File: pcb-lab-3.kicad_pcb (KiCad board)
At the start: 2 copper layers, 0 parts

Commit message: Approx layout of 1st circuit
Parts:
- added C1: 0.1u, local_footprints:0805_HS, F.Cu at (149.9, 45.7)
- added C2: 1u, local_footprints:1206_HS, F.Cu at (132.7, 40.6)
- added C3: 0.1u, local_footprints:0805_HS, F.Cu at (141.0, 36.8)
- added C301: 0.1u, local_footprints:0805_HS, F.Cu at (127.6, 98.1)
- added C302: 0.1u, local_footprints:0805_HS, F.Cu at (145.1, 80.0)
- added C303: 1u, local_footprints:1206_HS, F.Cu at (127.1, 92.1)
- added C304: 0.1u, local_footprints:0805_HS, F.Cu at (137.9, 87.8)
- added C305: 0.1u, local_footprints:0805_HS, F.Cu at (145.1, 77.1)
- added C4: 0.1u, local_footprints:0805_HS, F.Cu at (146.1, 36.8)
- added C401: 0.1u, local_footprints:0805_HS, F.Cu at (133.4, 111.6)
- added C402: 1u, local_footprints:1206_HS, F.Cu at (130.7, 104.3)
- added C403: 1u, local_footprints:1206_HS, F.Cu at (116.2, 121.3)
- added C404: 1u, local_footprints:1206_HS, F.Cu at (124.0, 113.0)
- added C405: 0.1u, local_footprints:0805_HS, F.Cu at (125.6, 120.6)
- added C406: 0.1u, local_footprints:0805_HS, F.Cu at (128.1, 116.8)
- added J1: USB_B_Micro, local_footprints:USB-micro-B_4-legs_Banggood, F.Cu at (121.9, 40.6)
- added J2: Conn_01x02, local_footprints:Pin_Header_Straight_1x02_Pitch2.54mm, F.Cu at (130.2, 39.4)
- added J3: Conn_01x02, local_footprints:Pin_Header_Straight_1x02_Pitch2.54mm, F.Cu at (161.9, 36.8)
- added J301: USB_B_Micro, local_footprints:USB-micro-B_4-legs_Banggood, F.Cu at (111.6, 92.7)
- added J302: USB_B_Micro, local_footprints:USB-micro-B_4-legs_Banggood, F.Cu at (111.6, 83.5)
- added J303: Conn_01x02, local_footprints:Pin_Header_Straight_1x02_Pitch2.54mm, F.Cu at (126.1, 88.7)
- added J304: Conn_01x02, local_footprints:Pin_Header_Straight_1x02_Pitch2.54mm, F.Cu at (122.5, 92.6)
- added J305: Conn_01x02, local_footprints:Pin_Header_Straight_1x02_Pitch2.54mm, F.Cu at (133.9, 80.0)
- added J306: Conn_01x02, local_footprints:Pin_Header_Straight_1x02_Pitch2.54mm, F.Cu at (137.5, 80.0)
- added J307: Conn_01x02, local_footprints:Pin_Header_Straight_1x02_Pitch2.54mm, F.Cu at (122.5, 86.5)
- added J308: Conn_01x02, local_footprints:Pin_Header_Straight_1x02_Pitch2.54mm, F.Cu at (141.1, 80.0)
- added J309: Conn_01x03_Female, local_footprints:Pin_Header_Straight_1x03_Pitch2.54mm, F.Cu at (127.7, 82.6)
- added J310: Conn_01x02_Female, local_footprints:Pin_Header_Straight_1x02_Pitch2.54mm, F.Cu at (133.9, 86.2)
- added J311: Conn_01x03_Female, local_footprints:Pin_Header_Straight_1x03_Pitch2.54mm, F.Cu at (118.9, 89.0)
- added J4: Conn_01x02, local_footprints:Pin_Header_Straight_1x02_Pitch2.54mm, F.Cu at (161.9, 41.9)
- added J401: USB_B_Micro, local_footprints:USB-micro-B_4-legs_Banggood, F.Cu at (111.6, 110.4)
- added J402: Conn_01x02, local_footprints:Pin_Header_Straight_1x02_Pitch2.54mm, F.Cu at (111.6, 122.7)
- added J403: Conn_01x02, local_footprints:Pin_Header_Straight_1x02_Pitch2.54mm, F.Cu at (126.1, 107.0)
- added J404: Conn_01x02, local_footprints:Pin_Header_Straight_1x02_Pitch2.54mm, F.Cu at (119.4, 115.7)
- added J405: Conn_01x03, local_footprints:Pin_Header_Straight_1x03_Pitch2.54mm, F.Cu at (122.5, 109.5)
- added J406: Conn_01x03_Female, local_footprints:Pin_Header_Straight_1x03_Pitch2.54mm, F.Cu at (118.9, 109.5)
- added J407: Conn_01x02, local_footprints:Pin_Header_Straight_1x02_Pitch2.54mm, F.Cu at (108.0, 122.7)
- added J5: Conn_01x03, local_footprints:Pin_Header_Straight_1x03_Pitch2.54mm, F.Cu at (142.2, 49.5)
- added J501: Conn_01x02, local_footprints:Pin_Header_Straight_1x02_Pitch2.54mm, F.Cu at (157.7, 107.0)
- added J502: Conn_01x02, local_footprints:Pin_Header_Straight_1x02_Pitch2.54mm, F.Cu at (161.3, 107.0)
- added J503: Conn_01x02, local_footprints:Pin_Header_Straight_1x02_Pitch2.54mm, F.Cu at (154.1, 107.0)
- added J6: Conn_01x04, local_footprints:Pin_Header_Straight_1x04_Pitch2.54mm, F.Cu at (123.2, 48.3)
- added JP1: SolderJumper_2_Open, Jumper:SolderJumper-2_P1.3mm_Open_RoundedPad1.0x1.5mm, F.Cu at (137.8, 41.9)
- added JP2: SolderJumper_2_Open, Jumper:SolderJumper-2_P1.3mm_Open_RoundedPad1.0x1.5mm, F.Cu at (151.1, 39.4)
- added JP301: SolderJumper_2_Open, Jumper:SolderJumper-2_P1.3mm_Open_RoundedPad1.0x1.5mm, F.Cu at (145.5, 91.0)
- added JP302: SolderJumper_2_Open, Jumper:SolderJumper-2_P1.3mm_Open_RoundedPad1.0x1.5mm, F.Cu at (140.9, 94.6)
- added JP303: SolderJumper_2_Open, Jumper:SolderJumper-2_P1.3mm_Open_RoundedPad1.0x1.5mm, F.Cu at (141.2, 91.0)
- added JP304: SolderJumper_2_Open, Jumper:SolderJumper-2_P1.3mm_Open_RoundedPad1.0x1.5mm, F.Cu at (136.3, 97.2)
- added JP401: SolderJumper_2_Open, Jumper:SolderJumper-2_P1.3mm_Open_RoundedPad1.0x1.5mm, F.Cu at (129.9, 120.0)
- added JP402: SolderJumper_2_Open, Jumper:SolderJumper-2_P1.3mm_Open_RoundedPad1.0x1.5mm, F.Cu at (140.1, 109.1)
- added JP403: SolderJumper_2_Open, Jumper:SolderJumper-2_P1.3mm_Open_RoundedPad1.0x1.5mm, F.Cu at (133.3, 114.8)
- added Q1: Q_NMOS_GSD, local_footprints:SOT-23_HS, F.Cu at (157.5, 40.6)
- added Q301: Q_NMOS_GSD, local_footprints:SOT-23_HS, F.Cu at (132.2, 90.2)
- added Q302: Q_NMOS_GSD, local_footprints:SOT-23_HS, F.Cu at (138.1, 84.1)
- added Q401: Q_NMOS_GSD, local_footprints:SOT-23_HS, F.Cu at (123.5, 116.9)
- added R1: 100k, local_footprints:0805_HS, F.Cu at (129.5, 48.3)
- added R2: 1k, local_footprints:0805_HS, F.Cu at (139.7, 41.9)
- added R3: 100k, local_footprints:0805_HS, F.Cu at (149.9, 50.2)
- added R301: 1k, local_footprints:0805_HS, F.Cu at (136.5, 94.0)
- added R302: 1k, local_footprints:0805_HS, F.Cu at (132.0, 96.8)
- added R303: 100k, local_footprints:0805_HS, F.Cu at (142.3, 87.8)
- added R304: 100k, local_footprints:0805_HS, F.Cu at (136.8, 90.7)
- added R305: 1, local_footprints:1210_HS, F.Cu at (109.0, 96.0)
- added R306: 1k, local_footprints:0805_HS, F.Cu at (132.1, 94.0)
- added R307: 1k, local_footprints:0805_HS, F.Cu at (142.6, 83.3)
- added R308: 100k, local_footprints:0805_HS, F.Cu at (127.6, 95.2)
- added R309: 1, local_footprints:1210_HS, F.Cu at (122.6, 96.2)
- added R4: 3.3k, local_footprints:0805_HS, F.Cu at (149.9, 52.7)
- added R401: 3.3k, local_footprints:0805_HS, F.Cu at (140.8, 104.1)
- added R402: 3.3k, local_footprints:0805_HS, F.Cu at (135.7, 108.7)
- added R403: 100k, local_footprints:0805_HS, F.Cu at (129.0, 113.9)
- added R404: 1k, local_footprints:0805_HS, F.Cu at (129.0, 111.0)
- added R405: 1k, local_footprints:0805_HS, F.Cu at (121.2, 120.6)
- added R406: 100k, local_footprints:0805_HS, F.Cu at (121.2, 123.5)
- added R407: 1, local_footprints:1210_HS, F.Cu at (130.7, 107.7)
- added R5: 1k, local_footprints:0805_HS, F.Cu at (151.1, 36.8)
- added R6: 100k, local_footprints:0805_HS, F.Cu at (156.2, 36.8)
- added R7: 1, local_footprints:1210_HS, F.Cu at (146.1, 51.4)
- added RV1: 50k, local_footprints:Conn_01x03_small, F.Cu at (138.4, 52.1)
- added RV301: 100k, local_footprints:Conn_01x03_small, F.Cu at (130.8, 79.6)
- added RV302: 10k, local_footprints:Conn_01x03_small, F.Cu at (118.4, 94.7)
- added RV401: 1k, local_footprints:Conn_01x03_small, F.Cu at (116.3, 115.8)
- added RV501: 100, local_footprints:Conn_01x03_small, F.Cu at (151.0, 106.5)
- added TP1: TestPoint, local_footprints:SMD-Pad_01x01, F.Cu at (135.9, 45.1)
- added TP401: TestPoint, local_footprints:SMD-Pad_01x01, F.Cu at (125.5, 123.3)
- added TP402: TestPoint, local_footprints:SMD-Pad_01x01, F.Cu at (137.7, 112.2)
- added U1: NCS2333, local_footprints:SOIC-8_3.9x4.9mm_Pitch1.27mm_HS, F.Cu at (144.8, 43.2)
- added U2: MCP4011, local_footprints:SOIC-8_3.9x4.9mm_Pitch1.27mm_HS, F.Cu at (129.5, 52.1)
- added U301: NCS2333, local_footprints:SOIC-8_3.9x4.9mm_Pitch1.27mm_HS, F.Cu at (121.5, 78.9)
- added U302: INA181, local_footprints:SOT-23-6_HS, F.Cu at (114.3, 96.5)
- added U401: NCS2333, local_footprints:SOIC-8_3.9x4.9mm_Pitch1.27mm_HS, F.Cu at (110.6, 115.1)
- added U402: INA181, local_footprints:SOT-23-6_HS, F.Cu at (136.0, 105.0)
- added U501: BCR421U, local_footprints:SOT-23-6_HS, F.Cu at (165.7, 105.0)

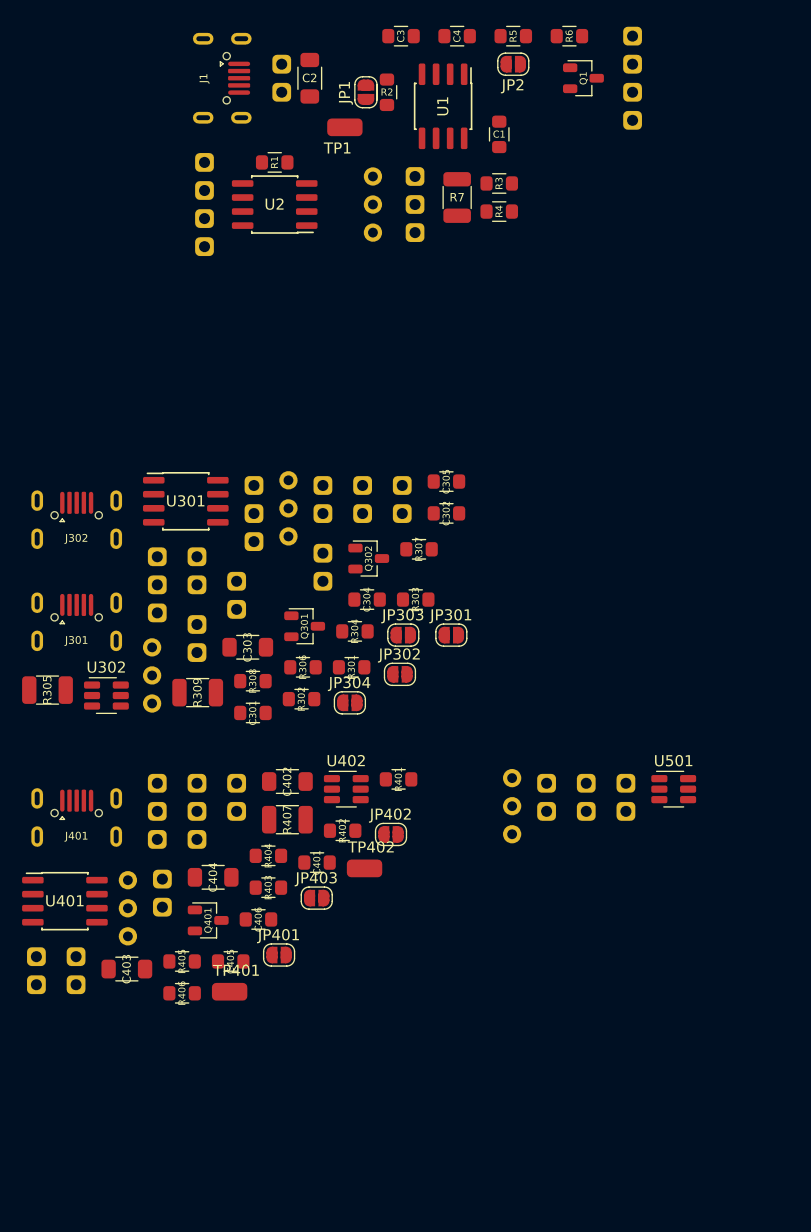
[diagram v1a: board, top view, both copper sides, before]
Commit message: Approx layout of all components / all circuits
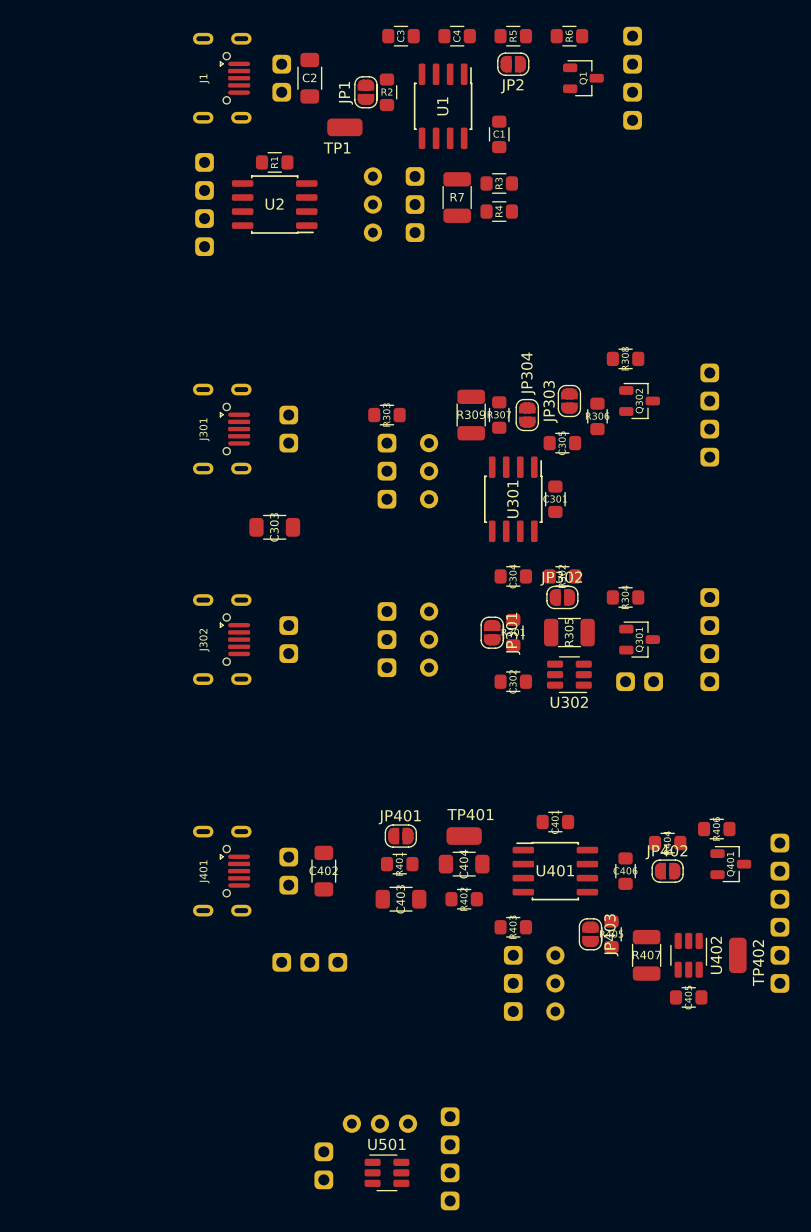
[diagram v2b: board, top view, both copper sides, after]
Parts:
- moved J407 67.3 mm to (175.3, 120.0), turned to 180 degrees
- moved J404 55.9 mm to (175.3, 114.9), turned to 180 degrees
- moved R406 50.6 mm to (169.5, 108.6)
- moved J403 49.2 mm to (175.3, 109.9), turned to 180 degrees
- moved Q401 47.6 mm to (170.8, 111.8)
- moved R305 47.5 mm to (156.2, 90.8), turned to 180 degrees
- moved J307 46.4 mm to (168.9, 87.6), turned to 180 degrees
- moved R308 44.6 mm to (161.3, 66.0), turned to 180 degrees
- moved U401 44.5 mm to (154.9, 112.4)
- moved U501 43.4 mm to (139.7, 139.7)
- moved U302 41.9 mm to (156.2, 94.6), turned to 180 degrees
- moved C405 41.6 mm to (167.0, 123.8), turned to 180 degrees
- moved RV401 39.3 mm to (154.9, 122.6)
- moved R405 38.9 mm to (160.0, 118.1), turned to 90 degrees
- moved J501 38.9 mm to (134.0, 137.8), turned to 180 degrees
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
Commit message: Tune footprints, reimport netlist
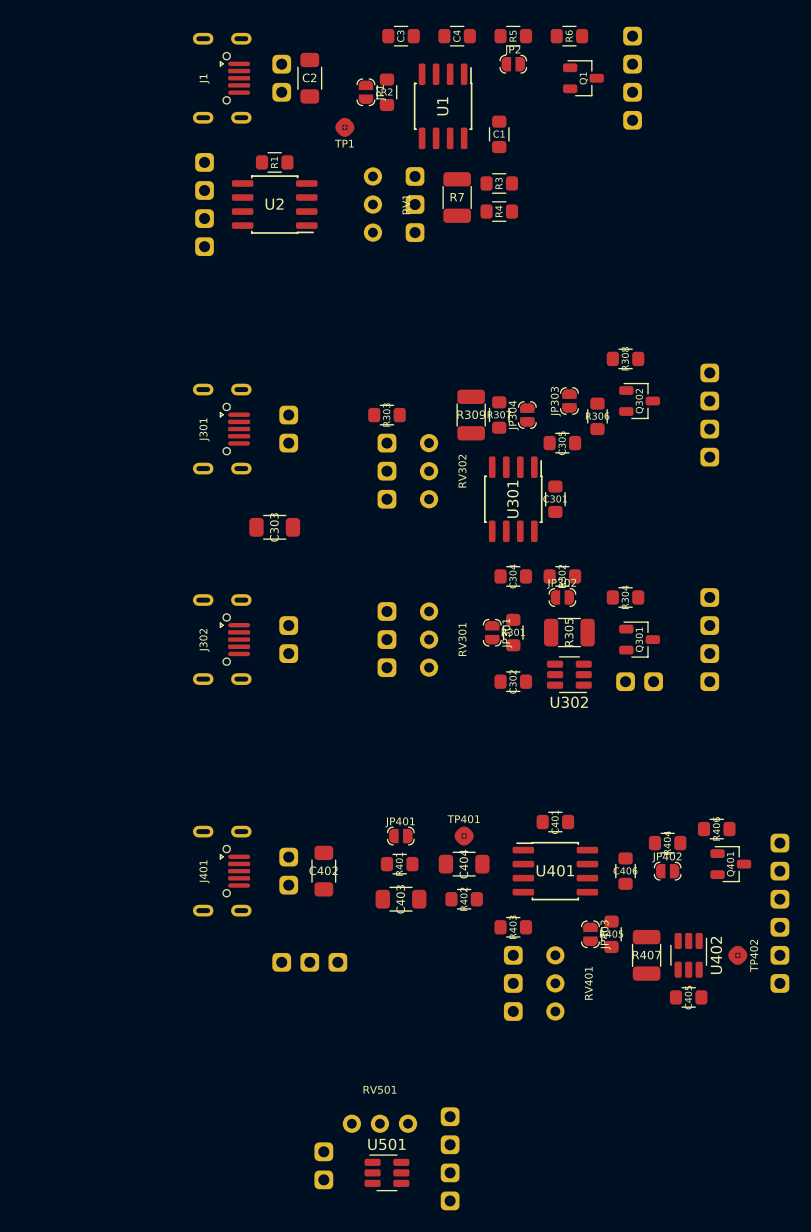
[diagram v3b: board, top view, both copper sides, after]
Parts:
- JP1, JP2, JP301, JP302, JP303, JP304, JP401, JP402, JP403: footprint Jumper:SolderJumper-2_P1.3mm_Open_RoundedPad1.0x1.5mm -> local_footprints:SolderJumper-2_P1.3mm_Open
- RV1, RV301, RV302, RV401, RV501: footprint local_footprints:Conn_01x03_small -> local_footprints:RV-Pot_3-pin_2.54mm
- TP1, TP401, TP402: footprint local_footprints:SMD-Pad_01x01 -> local_footprints:SMD-TestPoint_01x01

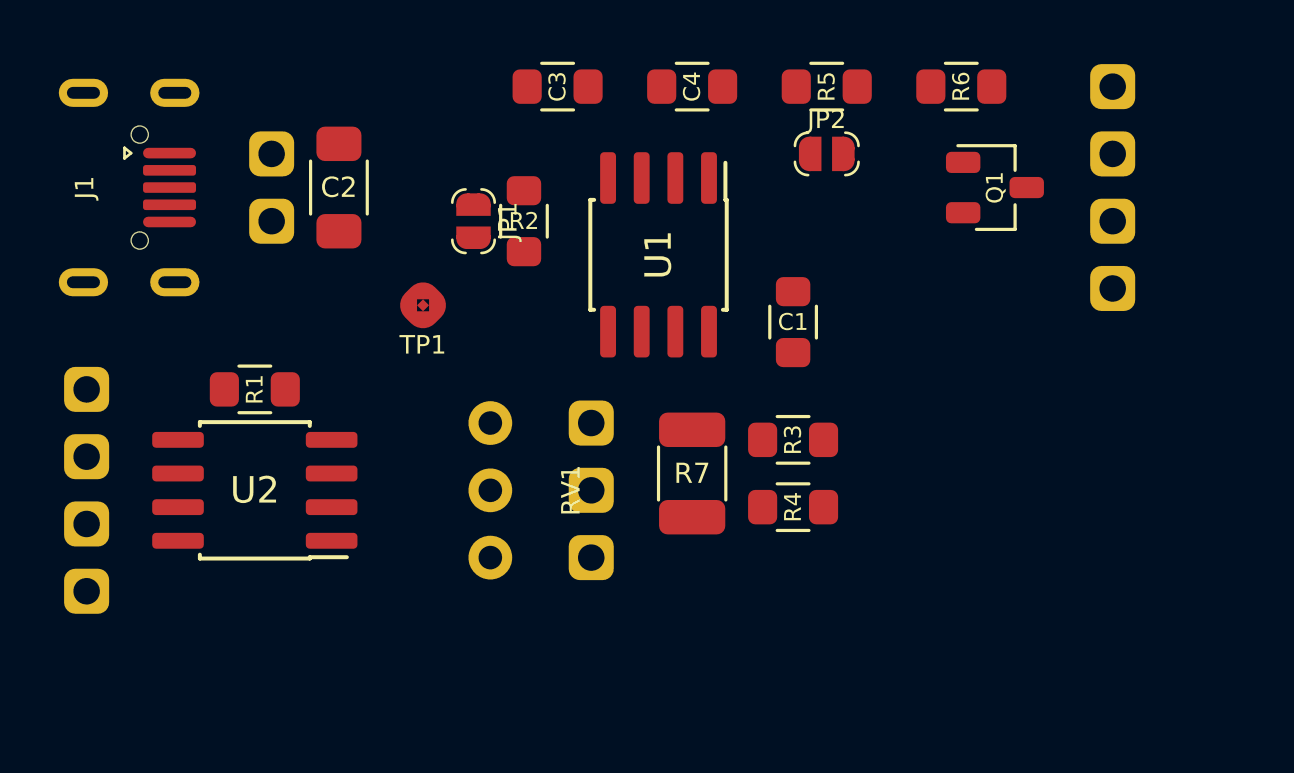
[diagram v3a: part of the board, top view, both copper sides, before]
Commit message: Complete routing (except GND) of 1st circuit
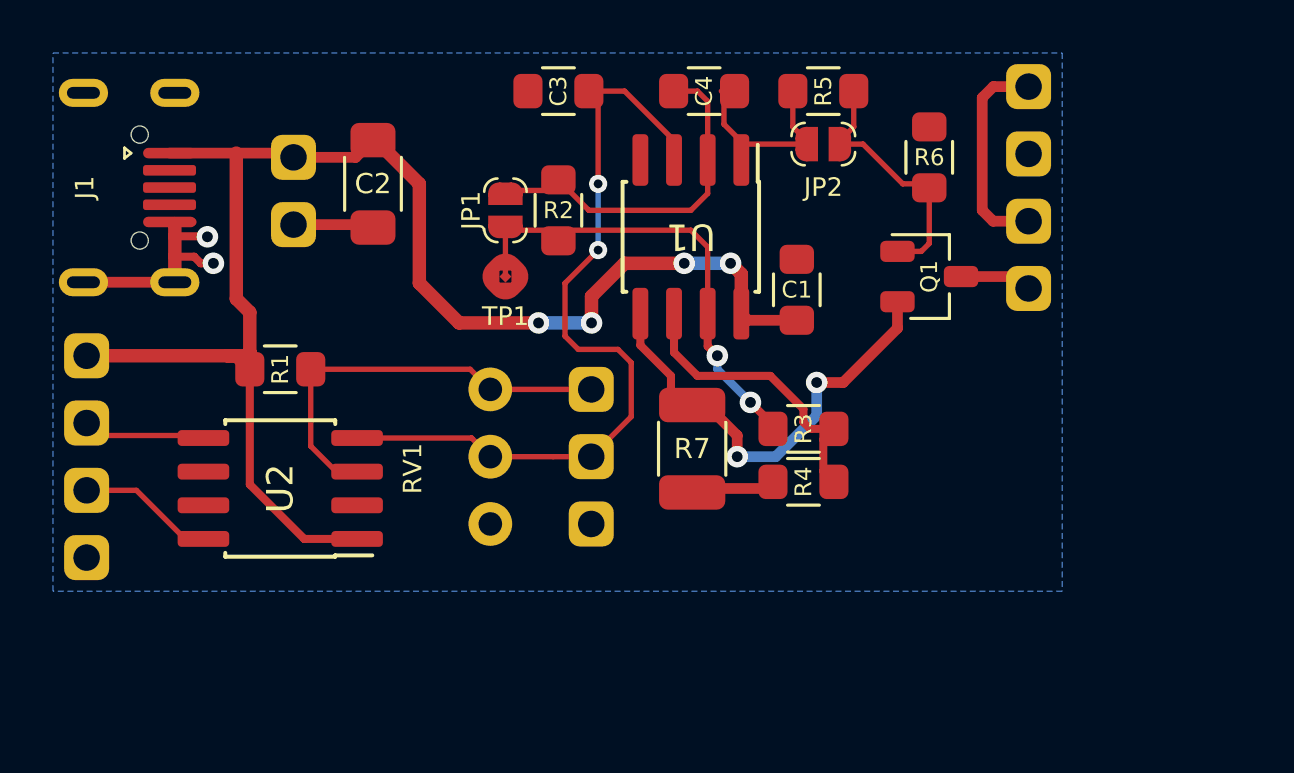
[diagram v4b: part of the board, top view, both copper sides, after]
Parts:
- moved Q1 4.18 mm to (155.0, 44.0)
- moved TP1 3.29 mm to (139.0, 44.0)
- moved J3 3.18 mm to (158.8, 36.8)
- moved J4 3.18 mm to (158.8, 41.9)
- moved R6 2.93 mm to (155.0, 39.5), turned to 270 degrees
- moved U1 1.40 mm to (146.0, 42.5)
- moved R2 1.36 mm to (141.0, 41.5)
- moved C2 1.29 mm to (134.0, 40.5)
- moved JP1 1.27 mm to (139.0, 41.5)
- moved J5 1.27 mm to (142.2, 48.3)
- moved RV1 1.27 mm to (138.4, 50.8)
- moved J6 1.27 mm to (123.2, 47.0)
- moved C1 1.23 mm to (150.0, 44.5)
- moved R1 1.22 mm to (130.5, 47.5)
- moved R4 1.03 mm to (150.2, 51.8)
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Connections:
- J6 pad 2: CTRL_UD -> CTRL_~CS
- J6 pad 3: CTRL_~CS -> CTRL_UD
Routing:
- net +5V: track 0.00 -> 57.3 mm, vias 0 -> 4
- net /2-OpAmp constant current/W: track 0.00 -> 31.1 mm, vias 0 -> 2
- net Net-(JP1-Pad2): track 0.00 -> 17.7 mm, vias 0 -> 2
- net Net-(Q1-Pad2): track 0.00 -> 16.3 mm, vias 0 -> 2
- net /2-OpAmp constant current/A: track 0.00 -> 16.0 mm
- net GND: track 0.00 -> 15.9 mm, vias 0 -> 2
- net Net-(C4-Pad2): track 0.00 -> 13.5 mm
- net Net-(R3-Pad1): track 0.00 -> 11.7 mm
- net Net-(JP2-Pad2): track 0.00 -> 9.66 mm
- net LOAD1+: track 0.00 -> 8.09 mm
- net Net-(C4-Pad1): track 0.00 -> 7.47 mm
- net CTRL_UD: track 0.00 -> 5.17 mm
- net CTRL_~CS: track 0.00 -> 4.64 mm
- net LOAD1-: track 0.00 -> 2.74 mm
- added copper zone on B.Cu, net GND
